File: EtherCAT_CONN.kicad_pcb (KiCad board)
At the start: 2 copper layers, 21 x 27 mm, 28 parts, among them CN1 5019530507, CN2 5019530507, J2 Conn_01x12, U1 SRV05-4, U2 SRV05-4

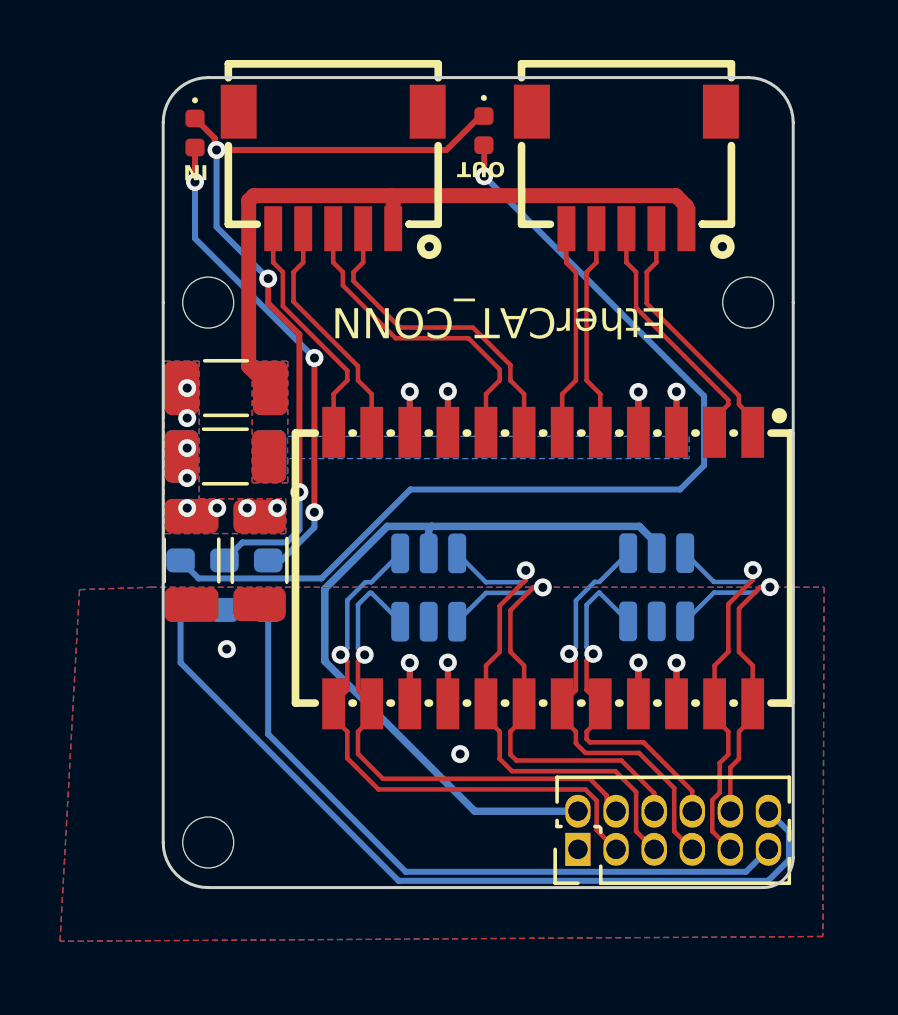
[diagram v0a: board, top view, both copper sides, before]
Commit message: Change routings
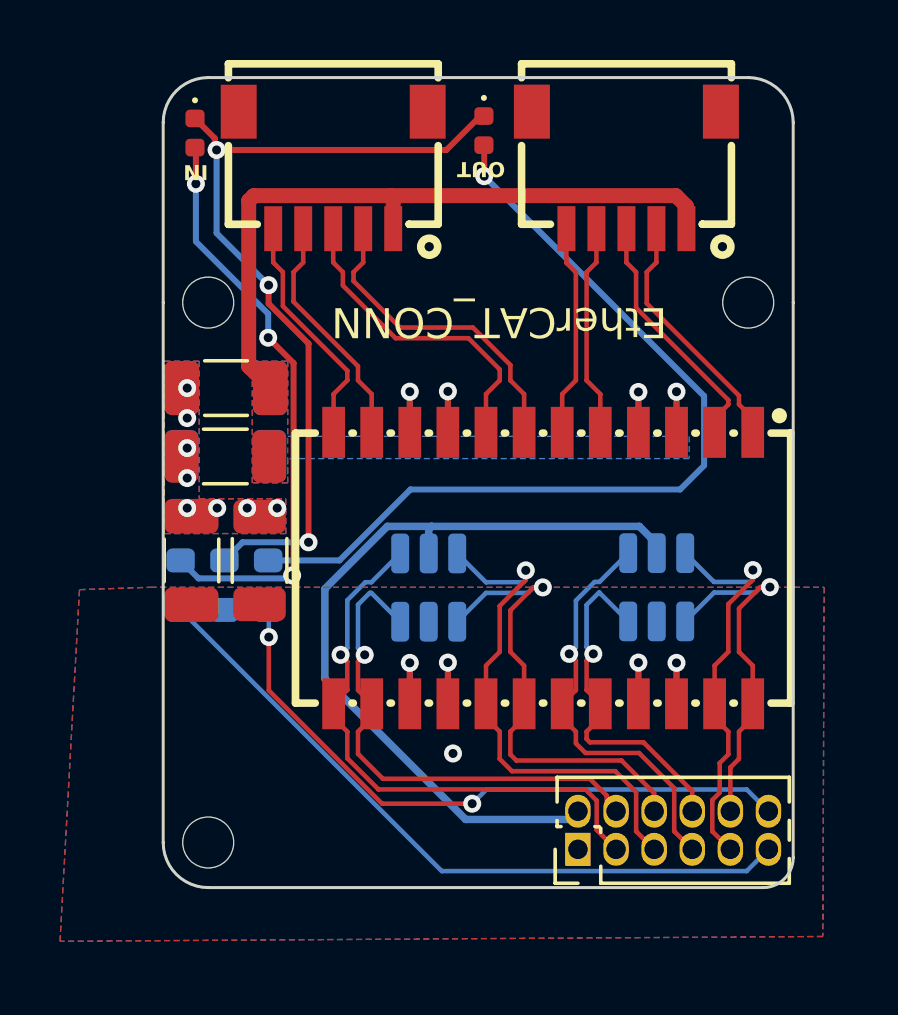
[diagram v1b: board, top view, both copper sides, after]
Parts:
- moved R8 2.92 mm to (146.8, 97.6)
- moved R9 2.92 mm to (149.7, 97.6)
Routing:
- net /CONN/P1_ACT: track 27.2 -> 21.4 mm, vias 0 -> 2
- net Net-(D2-A): track 33.0 -> 29.6 mm
- net Net-(D1-A): track 16.3 -> 19.7 mm
- net Net-(D1-K): track 27.5 -> 28.1 mm
- net A3V3: track 26.3 -> 26.9 mm
- net GND: vias 2 -> 1

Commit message: All 0603 version
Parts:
- C1, C2, C3, C4: footprint Capacitor_SMD:C_0402_1005Metric -> Capacitor_SMD:C_0603_1608Metric
- D1, D2: footprint LED_SMD:LED_0402_1005Metric -> LED_SMD:LED_0603_1608Metric
- R2, R3, R4, R5: footprint Resistor_SMD:R_0402_1005Metric -> Resistor_SMD:R_0603_1608Metric
- moved D2 1.69 mm to (156.8, 84.1)
- moved D1 1.62 mm to (147.0, 84.1)
- moved C4 0.71 mm to (163.4, 102.2)
- moved C3 0.71 mm to (161.9, 102.2)
- moved C1 0.42 mm to (154.3, 101.9)
- moved C2 0.42 mm to (155.8, 101.9)
- moved R2 0.12 mm to (154.3, 92.5)
- moved R3 0.11 mm to (155.8, 92.5)
- moved R4 0.10 mm to (161.9, 92.5)
- moved R5 0.10 mm to (163.4, 92.5)
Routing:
- net Net-(C7-Pad2): track 23.2 -> 20.3 mm, vias 0 -> 3
- net /CONN/P0_ACT: track 23.5 -> 25.1 mm
- net A3V3: track 26.9 -> 28.1 mm
- net Net-(D1-A): track 19.7 -> 18.5 mm, vias 3 -> 1
- net Net-(D1-K): track 28.1 -> 27.7 mm, vias 3 -> 1

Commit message: Official version
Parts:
- added H4: MountingHole, EXTRA IC:M1.6, F.Cu at (165.7, 106.2)
- added J1: Conn_01x20, Connector_PinHeader_1.27mm:ECAT_20pin, F.Cu at (156.7, 105.6)
- C5, R1: moved to B.Cu
- H1, H2, H3: footprint EXTRA IC:MountingHole_1.7mm_M1.6 -> EXTRA IC:M1.6
- J2: value Conn_01x12 -> Conn_01x06; footprint Connector_PinHeader_1.27mm:ECAT -> Connector_JST:JST_SH_BM06B-SRSS-TB_1x06-1MP_P1.00mm_Vertical
- moved R9 16.9 mm to (166.5, 95.5)
- moved R10 16.9 mm to (165.0, 95.5)
- moved R8 16.9 mm to (163.6, 95.5)
- moved J2 16.2 mm to (148.3, 99.3)
- moved R1 2.30 mm to (147.1, 96.7)
- moved C5 2.24 mm to (149.4, 96.7)
- moved U1 1.92 mm to (160.7, 97.7)
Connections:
- J2 pad 1: GND -> /SWCLK
- J2 pad 2: A3V3 -> /SWDIO
- J2 pad 3: /CONN/P1_TXOP -> /USART_RX
- J2 pad 4: /CONN/P1_TXON -> /USART_TX
- J2 pad 5: /CONN/P1_RXIP -> GND
- J2 pad 6: /CONN/P1_RXIN -> +5V
- L1 pad 1: /CONN/P0_MRXIN -> /CONN/P0_MRXIP
- L1 pad 11: /CONN/P1_MTXON -> /CONN/P1_MTXOP
- L1 pad 12: /CONN/P1_MTXOP -> /CONN/P1_MTXON
- L1 pad 13: /CONN/P1_TXOP -> /CONN/P1_TXON
- L1 pad 14: /CONN/P1_TXON -> /CONN/P1_TXOP
- L1 pad 17: /CONN/P1_RXIP -> /CONN/P1_RXIN
- L1 pad 18: /CONN/P1_RXIN -> /CONN/P1_RXIP
- L1 pad 19: /CONN/P0_TXOP -> /CONN/P0_TXON
- L1 pad 2: /CONN/P0_MRXIP -> /CONN/P0_MRXIN
- L1 pad 20: /CONN/P0_TXON -> /CONN/P0_TXOP
- L1 pad 23: /CONN/P0_RXIP -> /CONN/P0_RXIN
- L1 pad 24: /CONN/P0_RXIN -> /CONN/P0_RXIP
- L1 pad 5: /CONN/P0_MTXON -> /CONN/P0_MTXOP
- L1 pad 6: /CONN/P0_MTXOP -> /CONN/P0_MTXON
- L1 pad 7: /CONN/P1_MRXIN -> /CONN/P1_MRXIP
- L1 pad 8: /CONN/P1_MRXIP -> /CONN/P1_MRXIN
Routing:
- net /CONN/P0_ACT: track 25.1 -> 10.6 mm
- net A3V3: track 28.1 -> 16.2 mm, vias 0 -> 2
- net Net-(D2-A): track 29.6 -> 17.6 mm
- net /CONN/P1_ACT: track 21.4 -> 11.7 mm, vias 2 -> 0
- net +5V: track 0.00 -> 9.42 mm, vias 0 -> 1
- net /USART_TX: track 0.00 -> 8.61 mm, vias 0 -> 1
- net /USART_RX: track 0.00 -> 8.36 mm
- net /CONN/P1_RXIN: track 15.8 -> 9.43 mm
- net Net-(D1-A): track 18.5 -> 24.6 mm
- net /SWCLK: track 0.00 -> 5.84 mm
- net /SWDIO: track 0.00 -> 5.56 mm
- net /CONN/P1_RXIP: track 17.2 -> 11.7 mm
- net /CONN/P0_RXIP: track 13.5 -> 15.6 mm
- net Net-(D1-K): track 27.7 -> 26.1 mm
- net Net-(C7-Pad2): track 20.3 -> 18.7 mm
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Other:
- outline, holes or cut-outs redrawn

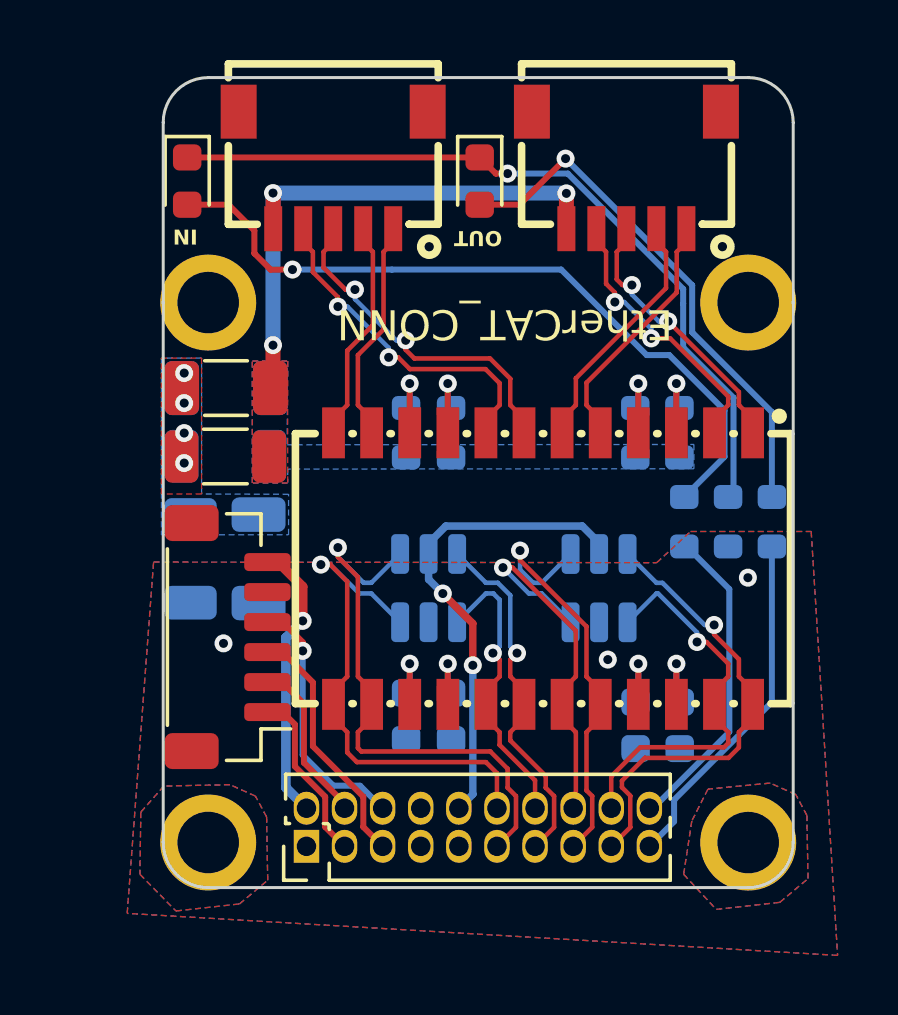
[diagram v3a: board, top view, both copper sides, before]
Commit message: Fixed LED_IN and LED_OUT bug
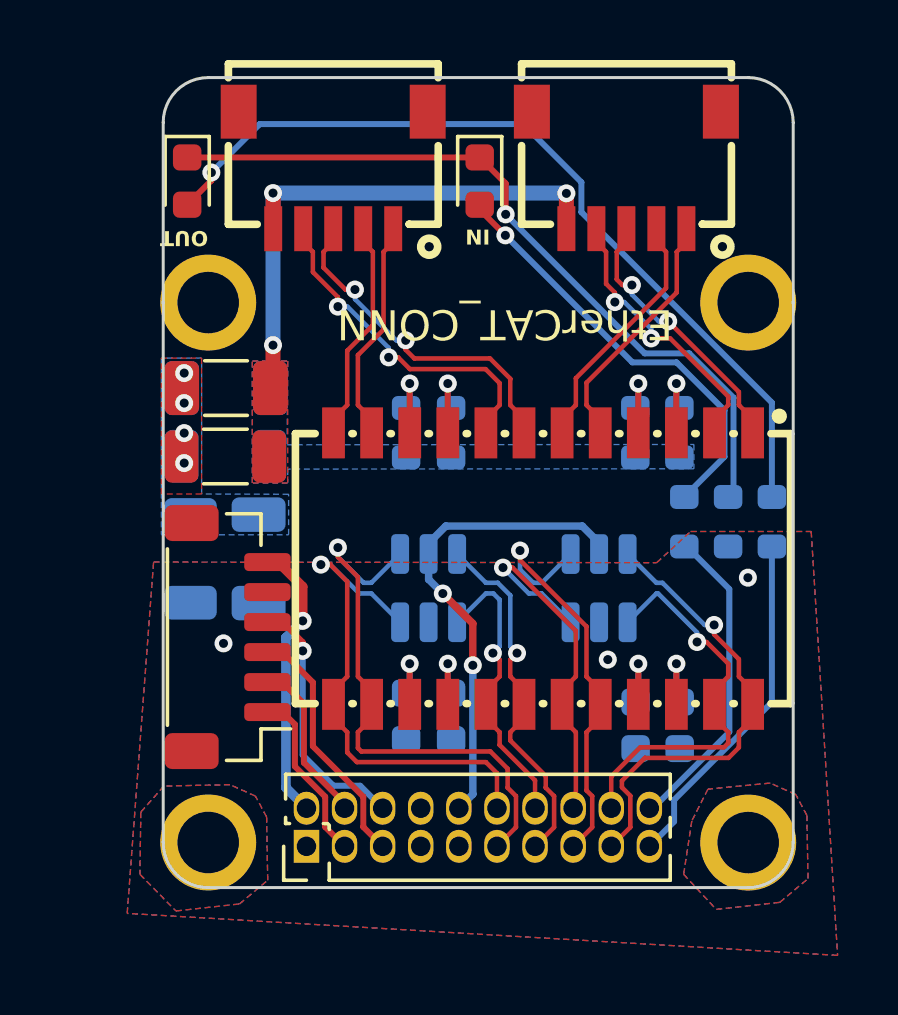
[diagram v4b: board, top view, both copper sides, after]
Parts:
- moved D1 9.75 mm to (156.8, 84.1)
- moved D2 9.75 mm to (147.0, 84.1)
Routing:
- net Net-(D2-A): track 17.6 -> 28.3 mm
- net Net-(D1-A): track 24.6 -> 14.5 mm
- net Net-(D1-K): track 26.1 -> 25.5 mm
